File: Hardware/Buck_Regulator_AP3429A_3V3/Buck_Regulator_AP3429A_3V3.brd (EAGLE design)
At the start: 25.4 x 25.4 mm, 54 parts, among them J1 Screw Terminal, J2 POWER_JACKPOWER_JACK_SLOT_COM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, J3 Breakout Headers, U1 AP3429/A

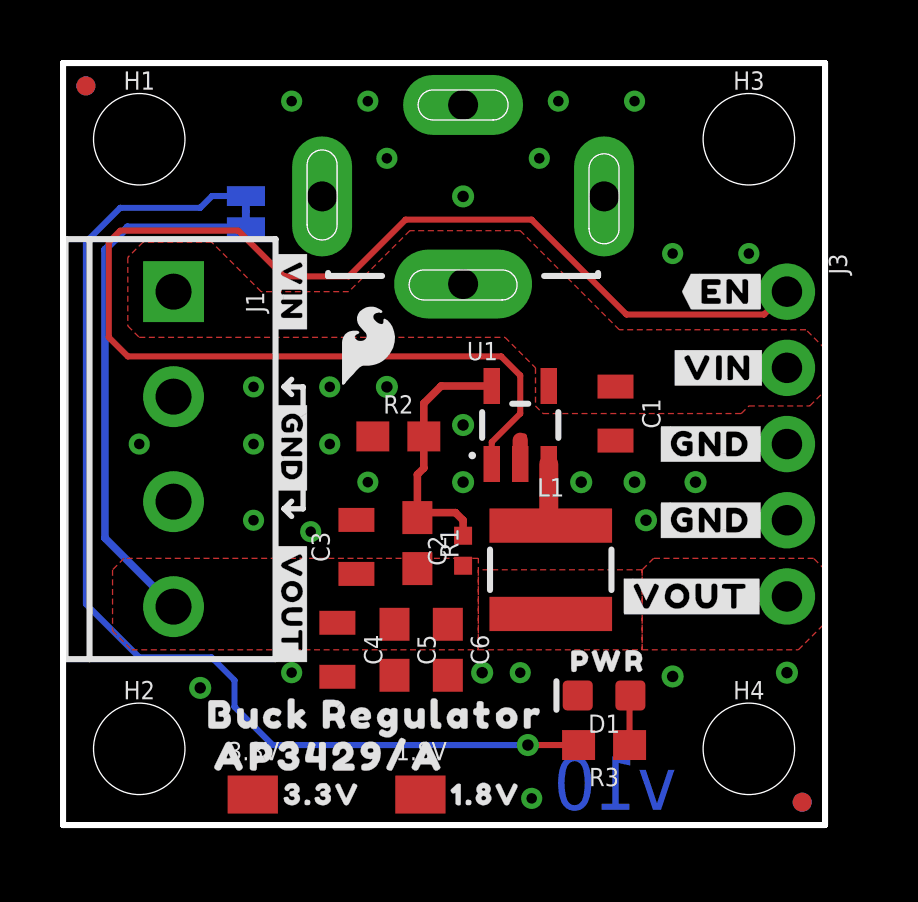
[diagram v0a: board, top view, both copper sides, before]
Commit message: V11 Design Update
Added 100k resistor to pull EN high to VIN for an easier plug and play application.
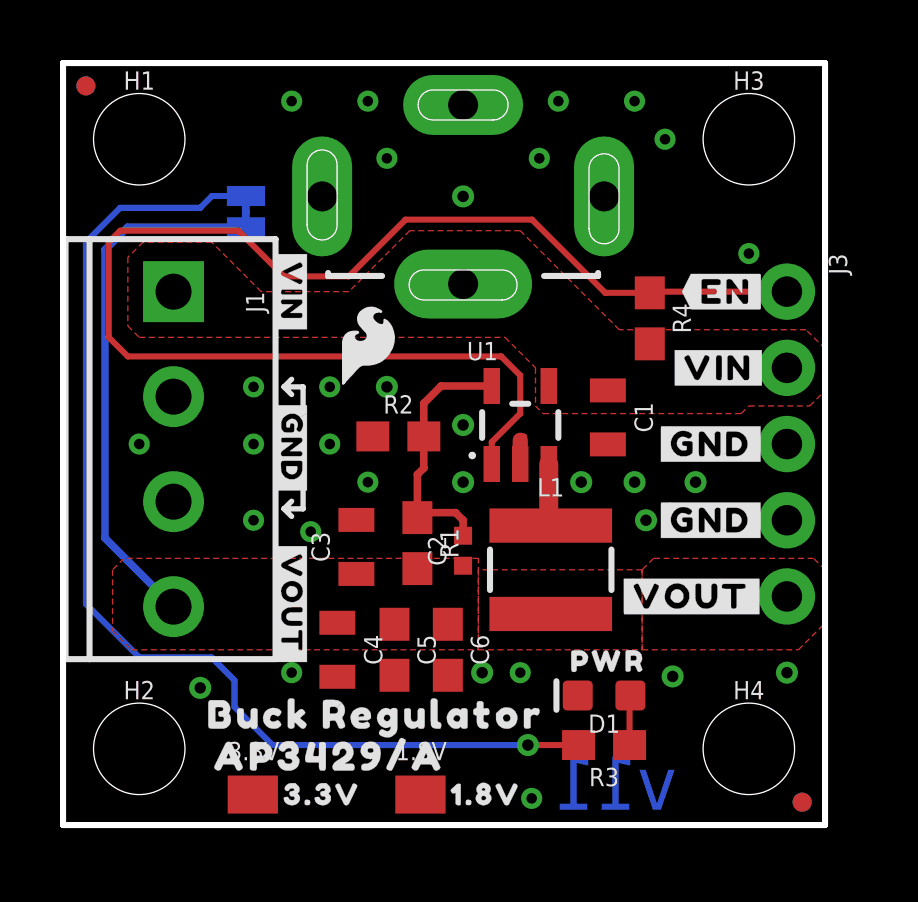
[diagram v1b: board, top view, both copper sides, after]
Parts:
- added R4: 100k, SparkFun-Resistors:0603
- moved C1 0.28 mm to (18.2, 13.6)
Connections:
- net EN: now also R4.1
- net VIN: now also R4.2
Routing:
- net EN: track 46.6 -> 46.0 mm
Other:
- board text added: "v11"
- board text removed: "v10"
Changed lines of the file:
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@@
 <grid distance="0.05" unitdist="inch" unit="inch" style="lines" multiple="1" display="yes" altdistance="0.005" altunitdist="inch" altunit="inch"/>
 <layers>
-<layer number="1" name="Top" color="4" fill="1" visible="no" active="yes"/>
+<layer number="1" name="Top" color="4" fill="1" visible="yes" active="yes"/>
 <layer number="2" name="Route2" color="16" fill="1" visible="no" active="no"/>
 <layer number="15" name="Route15" color="23" fill="1" visible="no" active="no"/>
-<layer number="16" name="Bottom" color="1" fill="1" visible="no" active="yes"/>
+<layer number="16" name="Bottom" color="1" fill="1" visible="yes" active="yes"/>
 <layer number="17" name="Pads" color="2" fill="1" visible="yes" active="yes"/>
-<layer number="18" name="Vias" color="2" fill="1" visible="no" active="yes"/>
-<layer number="19" name="Unrouted" color="6" fill="1" visible="no" active="yes"/>
+<layer number="18" name="Vias" color="2" fill="1" visible="yes" active="yes"/>
+<layer number="19" name="Unrouted" color="6" fill="1" visible="yes" active="yes"/>
 <layer number="20" name="Dimension" color="24" fill="1" visible="yes" active="yes"/>
-<layer number="21" name="tPlace" color="16" fill="1" visible="no" active="yes"/>
-<layer number="22" name="bPlace" color="14" fill="1" visible="no" active="yes"/>
-<layer number="23" name="tOrigins" color="15" fill="1" visible="no" active="yes"/>
-<layer number="24" name="bOrigins" color="15" fill="1" visible="no" active="yes"/>
+<layer number="21" name="tPlace" color="16" fill="1" visible="yes" active="yes"/>
+<layer number="22" name="bPlace" color="14" fill="1" visible="yes" active="yes"/>
+<layer number="23" name="tOrigins" color="15" fill="1" visible="yes" active="yes"/>
+<layer number="24" name="bOrigins" color="15" fill="1" visible="yes" active="yes"/>
 <layer number="25" name="tNames" color="7" fill="1" visible="no" active="yes"/>
 <layer number="26" name="bNames" color="7" fill="1" visible="no" active="yes"/>
@@
 <layer number="28" name="bValues" color="7" fill="1" visible="no" active="yes"/>
 <layer number="29" name="tStop" color="7" fill="3" visible="no" active="yes"/>
-<layer number="30" name="bStop" color="7" fill="6" visible="yes" active="yes"/>
+<layer number="30" name="bStop" color="7" fill="6" visible="no" active="yes"/>
 <layer number="31" name="tCream" color="7" fill="4" visible="no" active="yes"/>
 <layer number="32" name="bCream" color="7" fill="5" visible="no" active="yes"/>
@@
 <layer number="43" name="vRestrict" color="2" fill="10" visible="no" active="yes"/>
 <layer number="44" name="Drills" color="7" fill="1" visible="no" active="yes"/>
-<layer number="45" name="Holes" color="7" fill="1" visible="no" active="yes"/>
+<layer number="45" name="Holes" color="7" fill="1" visible="yes" active="yes"/>
 <layer number="46" name="Milling" color="3" fill="1" visible="no" active="yes"/>
-<layer number="47" name="Measures" color="7" fill="1" visible="yes" active="yes"/>
+<layer number="47" name="Measures" color="7" fill="1" visible="no" active="yes"/>
 <layer number="48" name="Document" color="7" fill="1" visible="no" active="yes"/>
-<layer number="49" name="Reference" color="38" fill="1" visible="yes" active="yes"/>
+<layer number="49" name="Reference" color="38" fill="1" visible="no" active="yes"/>
 <layer number="50" name="dxf" color="7" fill="1" visible="no" active="no"/>
 <layer number="51" name="tDocu" color="6" fill="1" visible="yes" active="yes"/>
@@
 <wire x1="7.366" y1="10.541" x2="7.62" y2="10.795" width="0.1778" layer="21"/>
 <wire x1="7.366" y1="10.541" x2="7.62" y2="10.287" width="0.1778" layer="21"/>
-<text x="20.447" y="0.508" size="1.778" layer="16" font="vector" ratio="15" rot="MR0">v10</text>
+<text x="20.447" y="0.508" size="1.778" layer="16" font="vector" ratio="15" rot="MR0">v11</text>
 <text x="12.7" y="-41.91" size="1.778" layer="51" font="vector" ratio="10" distance="15">M. Chodikov</text>
 <wire x1="5.334" y1="11.176" x2="5.334" y2="10.414" width="0.2032" layer="22"/>
@@
 <element name="FRAME1" library="SparkFun-Aesthetics" package="CREATIVE_COMMONS" value="FRAME-LEDGER" x="-13.97" y="-41.91" smashed="yes">
 <attribute name="DESIGNER" value="M. Chodikov" x="66.04" y="-54.61" size="1.778" layer="27" display="off"/>
-<attribute name="REV" value="v10" x="66.04" y="-54.61" size="1.778" layer="27" display="off"/>
+<attribute name="REV" value="v11" x="66.04" y="-54.61" size="1.778" layer="27" display="off"/>
 </element>
 <element name="L1" library="SparkFun-Coils" package="INDUCTOR_4X4MM" value="2.2μH" x="16.256" y="8.509" smashed="yes">
@@
 <element name="U$15" library="output" package="#VIN#3445" value="" x="5.334" y="17.78" smashed="yes" rot="MR90"/>
 <element name="U$14" library="output" package="#PWR#3451" value="" x="6.096" y="23.241" smashed="yes" rot="MR90"/>
-<element name="C1" library="SparkFun-Capacitors" package="0805" value="22uF" x="18.415" y="13.716" smashed="yes" rot="R270">
-<attribute name="NAME" x="19.304" y="13.716" size="0.6096" layer="25" font="vector" ratio="20" rot="R270" align="bottom-center"/>
-<attribute name="PROD_ID" value="CAP-14260" x="18.415" y="13.716" size="1.778" layer="27" font="vector" ratio="15" rot="R270" display="off"/>
-<attribute name="VALUE" x="17.526" y="13.716" size="0.6096" layer="27" font="vector" ratio="20" rot="R270" align="top-center"/>
+<element name="C1" library="SparkFun-Capacitors" package="0805" value="22uF" x="18.161" y="13.589" smashed="yes" rot="R270">
+<attribute name="NAME" x="19.05" y="13.589" size="0.6096" layer="25" font="vector" ratio="20" rot="R270" align="bottom-center"/>
+<attribute name="PROD_ID" value="CAP-14260" x="18.161" y="13.589" size="1.778" layer="27" font="vector" ratio="15" rot="R270" display="off"/>
+<attribute name="VALUE" x="17.272" y="13.589" size="0.6096" layer="27" font="vector" ratio="20" rot="R270" align="top-center"/>
 </element>
 <element name="C3" library="SparkFun-Capacitors" package="0805" value="22uF" x="9.779" y="9.271" smashed="yes" rot="R90">
@@
 <element name="J2" library="SparkFun-Connectors" package="POWER_JACK_PTH_SLOT_BOTH" value="POWER_JACKPOWER_JACK_SLOT_COMBO" x="13.335" y="24.003" smashed="yes" rot="R90"/>
 <element name="U$17" library="SparkFun-Aesthetics" package="ORDERING_INSTRUCTIONS" value="" x="31.75" y="25.4" smashed="yes"/>
+<element name="R4" library="SparkFun-Resistors" package="0603" value="100k" x="19.558" y="16.891" smashed="yes" rot="R270">
+<attribute name="NAME" x="20.32" y="16.891" size="0.6096" layer="25" font="vector" ratio="20" rot="R270" align="bottom-center"/>
+<attribute name="PROD_ID" value="RES-07828" x="19.558" y="16.891" size="1.778" layer="27" font="vector" ratio="15" rot="R270" display="off"/>
+<attribute name="VALUE" x="18.796" y="16.891" size="0.6096" layer="27" font="vector" ratio="20" rot="R270" align="top-center"/>
+</element>
 </elements>
 <signals>
@@
 </polygon>
 <contactref element="J2" pad="PWR"/>
+<contactref element="R4" pad="2"/>
 </signal>
 <signal name="GND">
@@
 <via x="7.62" y="5.08" extent="1-16" drill="0.35"/>
 <via x="22.86" y="19.05" extent="1-16" drill="0.35"/>
-<via x="20.32" y="19.05" extent="1-16" drill="0.35"/>
+<via x="20.066" y="22.86" extent="1-16" drill="0.35"/>
 <via x="6.35" y="12.7" extent="1-16" drill="0.35"/>
 <via x="2.54" y="12.7" extent="1-16" drill="0.35"/>
@@
 </signal>
 <signal name="EN">
-<contactref element="U1" pad="1"/>
 <contactref element="J3" pad="1"/>
-<wire x1="14.29" y1="12.0349" x2="14.29" y2="12.766" width="0.2032" layer="1"/>
 <wire x1="2.159" y1="15.621" x2="1.524" y2="16.256" width="0.2032" layer="1"/>
 <wire x1="14.29" y1="12.766" x2="15.24" y2="13.716" width="0.2032" layer="1"/>
@@
 <wire x1="1.524" y1="16.256" x2="1.524" y2="19.431" width="0.2032" layer="1"/>
 <wire x1="1.524" y1="19.431" x2="1.905" y2="19.812" width="0.2032" layer="1"/>
-<wire x1="15.61835" y1="20.1803" x2="18.78065" y2="17.018" width="0.2032" layer="1"/>
 <wire x1="1.905" y1="19.812" x2="5.842" y2="19.812" width="0.2032" layer="1"/>
 <wire x1="5.842" y1="19.812" x2="7.366" y2="18.288" width="0.2032" layer="1"/>
 <wire x1="7.366" y1="18.288" x2="9.525" y2="18.288" width="0.2032" layer="1"/>
 <wire x1="9.525" y1="18.288" x2="11.4173" y2="20.1803" width="0.2032" layer="1"/>
-<wire x1="11.4173" y1="20.1803" x2="15.61835" y2="20.1803" width="0.2032" layer="1"/>
-<wire x1="24.13" y1="17.78" x2="23.368" y2="17.018" width="0.2032" layer="1"/>
-<wire x1="23.368" y1="17.018" x2="18.78065" y2="17.018" width="0.2032" layer="1"/>
+<contactref element="U1" pad="1"/>
+<wire x1="14.29" y1="12.0349" x2="14.29" y2="12.766" width="0.2032" layer="1"/>
+<contactref element="R4" pad="1"/>
+<wire x1="18.073" y1="17.741" x2="19.558" y2="17.741" width="0.2032" layer="1"/>
+<wire x1="11.4173" y1="20.1803" x2="15.6337" y2="20.1803" width="0.2032" layer="1"/>
+<wire x1="15.6337" y1="20.1803" x2="18.073" y2="17.741" width="0.2032" layer="1"/>
+<wire x1="19.558" y1="17.741" x2="19.597" y2="17.78" width="0.2032" layer="1"/>
+<wire x1="19.597" y1="17.78" x2="24.13" y2="17.78" width="0.2032" layer="1"/>
 </signal>
 <signal name="N$3">
